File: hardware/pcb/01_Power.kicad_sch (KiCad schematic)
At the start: 11 parts, among them J1 USB_C_Receptacle_USB2.0_16P, U1 TLV62569DBV

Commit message: featt: make a 1.2 power rail from 3.3v
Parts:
- added C4, C7, C8: 22yF, symbol Device:C
- added C6: 10uF, symbol Device:C
- added L1: 2.2uH, symbol Device:L
- added R5, R6: 100k, symbol Device:R
- added U1: TLV62569DBV, Package_TO_SOT_SMD:SOT-23-5, symbol Regulator_Switching:TLV62569DBV
- renumbered U1 to U5
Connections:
- net +3V3: now also C6.1, U1.1 (EN), U1.4 (VIN)
- net GND: now also C4.2, C6.2, C7.2, R6.2, U1.2 (GND)
- new net: L1.1, U1.3 (SW)
- new net: C8.1, R5.2, R6.1, U1.5 (FB)
- new net +1V2: C4.1, C7.1, C8.2, L1.2, R5.1

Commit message: feat: the power circuit is fully made with all rails
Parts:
- added C10, C12: 1uF, symbol Device:C
- added C11, C13: 2.2uF, symbol Device:C
- added U2: TLV73325PDBV, Package_TO_SOT_SMD:SOT-23-5, symbol Regulator_Linear:TLV73325PDBV
- added U3: TLV73318PDBV, Package_TO_SOT_SMD:SOT-23-5, symbol Regulator_Linear:TLV73318PDBV
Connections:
- net +3V3: now also C10.1, C12.1, U2.1 (IN), U2.3 (EN), U3.1 (IN), U3.3 (EN)
- net GND: now also C10.2, C11.2, C12.2, C13.2, U2.2 (GND)
- new net +1V8: C13.1, U3.5 (OUT)
- new net +2V5: C11.1, U2.5 (OUT)

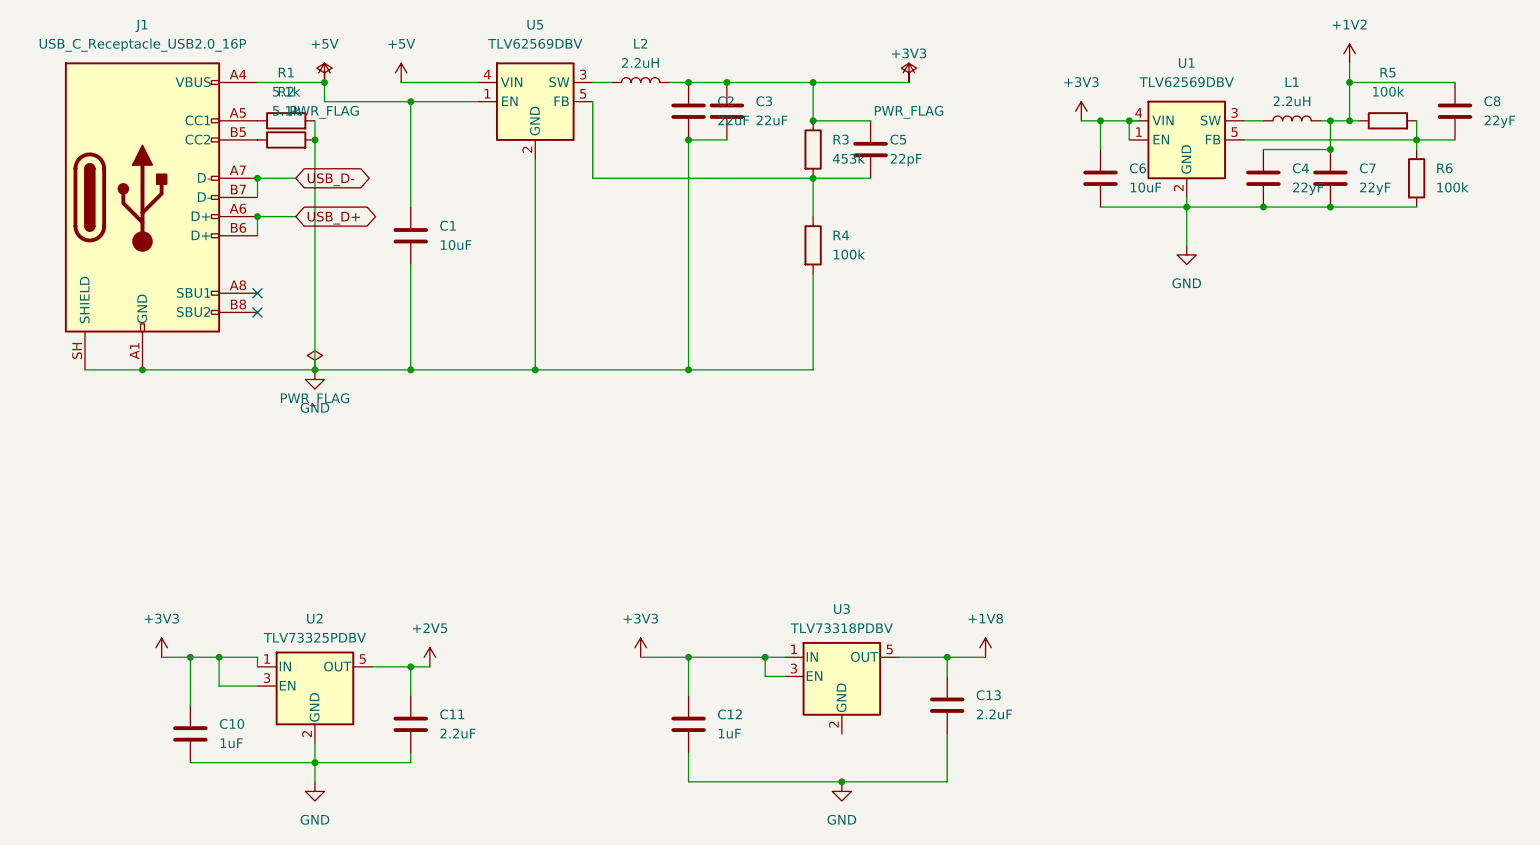
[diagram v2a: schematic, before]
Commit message: fix(power): resolve ERC violations and correct feedback capacitor values
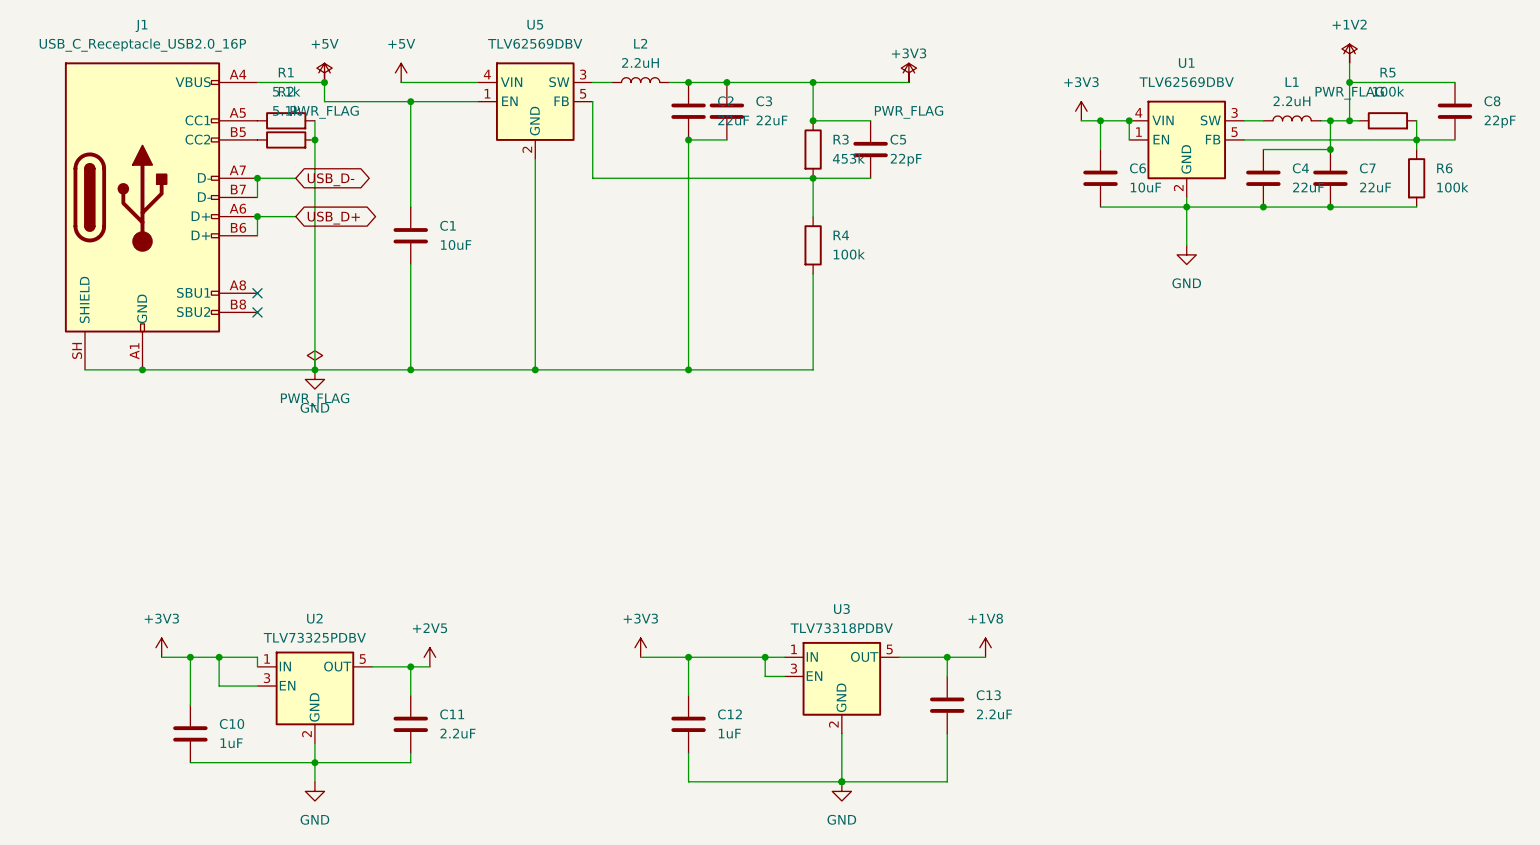
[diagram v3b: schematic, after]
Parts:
- C4, C7: value 22yF -> 22uF
- C8: value 22yF -> 22pF
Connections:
- net GND: now also U3.2 (GND)
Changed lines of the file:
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@@
 	(wire
 		(pts
-			(xy 153.67 72.39) (xy 154.94 72.39)
-		)
-		(stroke
-			(width 0)
-			(type default)
-		)
-	)
-	(wire
-		(pts
 			(xy 168.91 72.39) (xy 171.45 72.39)
 		)
@@
 			)
 		)
-		(property "Value" "22yF"
+		(property "Value" "22pF"
 			(at 200.66 72.3899 0)
 			(show_name no)
@@
 			)
 		)
-		(property "Value" "22yF"
+		(property "Value" "22uF"
 			(at 184.15 81.2799 0)
 			(show_name no)
@@
 			)
 		)
-		(property "Value" "22yF"
+		(property "Value" "22uF"
 			(at 175.26 81.2799 0)
 			(show_name no)
@@
 					(unit 1)
 				)
+			)
+		)
+	)
+	(wire
+		(pts
+			(xy 115.57 153.67) (xy 115.57 160.02)
+		)
+		(stroke
+			(width 0)
+			(type default)
+		)
+	)
+	(junction (at 115.57 160.02) (diameter 0) (color 0 0 0 0))
+	(symbol
+		(lib_id "power:PWR_FLAG")
+		(at 182.88 64.77 0)
+		(unit 1)
+		(exclude_from_sim no)
+		(in_bom yes)
+		(on_board yes)
+		(in_pos_files yes)
+		(dnp no)
+		(fields_autoplaced yes)
+		(property "Reference" "#FLG04"
+			(at 182.88 66.675 0)
+			(hide yes)
+			(show_name no)
+			(effects
+				(font
+					(size 1.27 1.27)
+				)
+			)
+		)
+		(property "Value" "PWR_FLAG"
+			(at 182.88 68.58 0)
+			(show_name no)
+			(effects
+				(font
+					(size 1.27 1.27)
+				)
+			)
+		)
+		(property "Footprint" ""
+			(at 182.88 64.77 0)
+			(hide yes)
+			(show_name no)
+			(effects
+				(font
+					(size 1.27 1.27)
+				)
+			)
+		)
+		(property "Datasheet" ""
+			(at 182.88 64.77 0)
+			(hide yes)
+			(show_name no)
+			(effects
+				(font
+					(size 1.27 1.27)
+				)
+			)
+		)
+		(property "Description" ""
+			(at 182.88 64.77 0)
+			(hide yes)
+			(show_name no)
+			(effects
+				(font
+					(size 1.27 1.27)
+				)
+			)
+		)
+		(pin "1"
+		)
+		(instances
+			(project "beanx5"
+				(path "/af63fa6e-973d-4760-8f53-35b43d2ef866/859f5aff-bcd5-4fba-93b3-4ce3a57d0421"
+					(reference "#FLG04")
+					(unit 1)
+				)

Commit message: feat: add power rails to the fpga gowin arora v family symbol
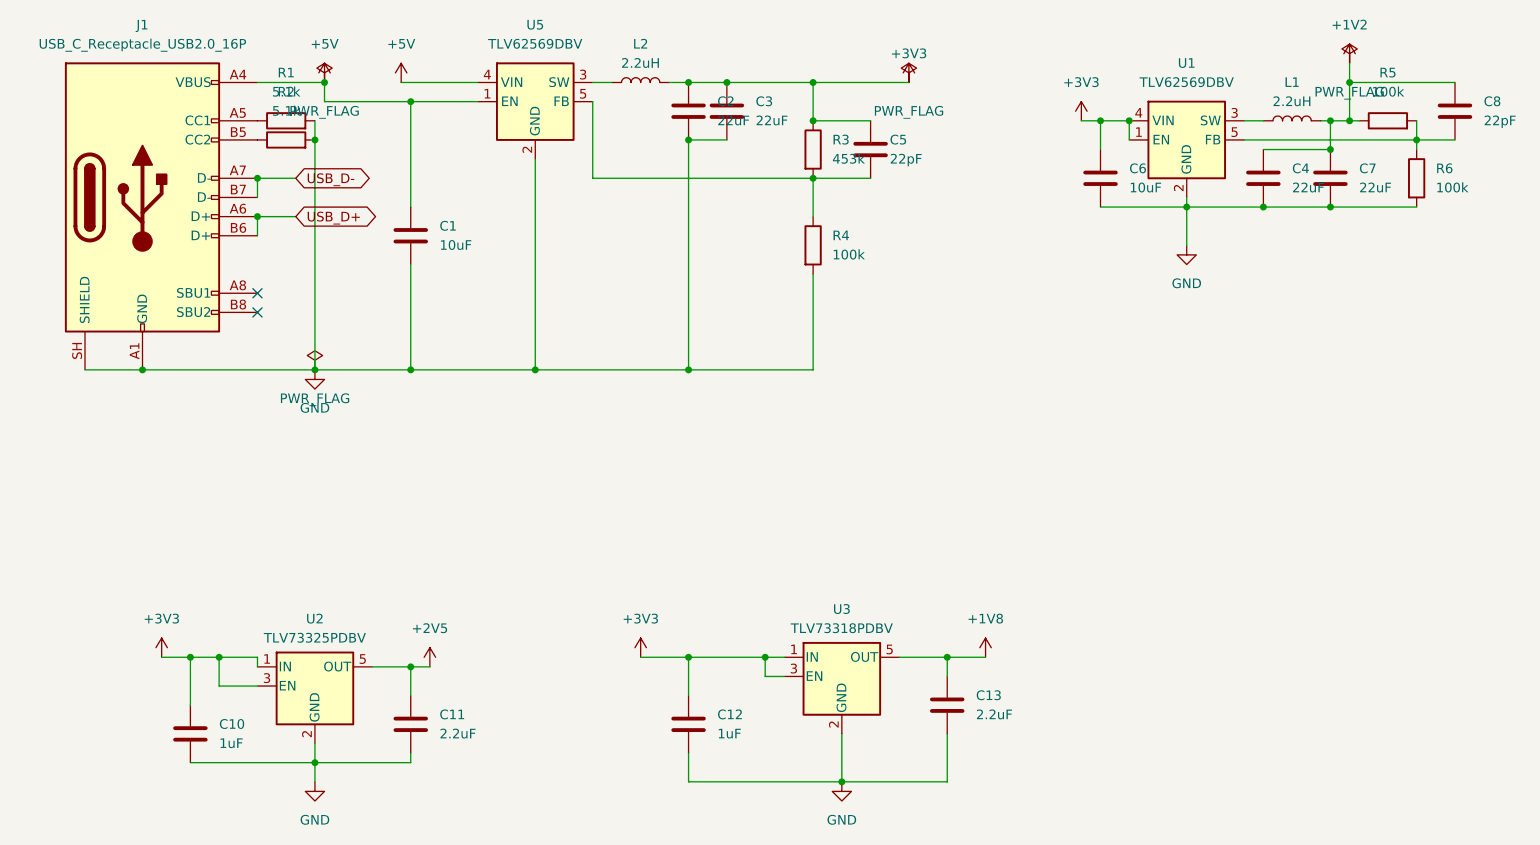
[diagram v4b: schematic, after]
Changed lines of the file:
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@@
 	(wire
 		(pts
-			(xy 45.72 105.41) (xy 74.93 105.41)
+			(xy 45.72 105.41) (xy 58.42 105.41)
 		)
 		(stroke
@@
 	(wire
 		(pts
+			(xy 58.42 69.85) (xy 67.31 69.85)
+		)
+		(stroke
+			(width 0)
+			(type default)
+		)
+	)
+	(wire
+		(pts
 			(xy 25.4 143.51) (xy 29.21 143.51)
 		)
@@
 	(wire
 		(pts
-			(xy 149.86 83.82) (xy 171.45 83.82)
+			(xy 149.86 83.82) (xy 161.29 83.82)
 		)
 		(stroke
@@
 	(wire
 		(pts
+			(xy 161.29 83.82) (xy 171.45 83.82)
+		)
+		(stroke
+			(width 0)
+			(type default)
+		)
+	)
+	(wire
+		(pts
 			(xy 95.25 67.31) (xy 100.33 67.31)
 		)
@@
 	(wire
 		(pts
-			(xy 46.99 69.85) (xy 67.31 69.85)
+			(xy 46.99 69.85) (xy 58.42 69.85)
 		)
 		(stroke
@@
 	(wire
 		(pts
+			(xy 58.42 105.41) (xy 74.93 105.41)
+		)
+		(stroke
+			(width 0)
+			(type default)
+		)
+	)
+	(wire
+		(pts
 			(xy 111.76 67.31) (xy 111.76 72.39)
 		)
@@
 	(wire
 		(pts
+			(xy 115.57 153.67) (xy 115.57 160.02)
+		)
+		(stroke
+			(width 0)
+			(type default)
+		)
+	)
+	(wire
+		(pts
 			(xy 74.93 77.47) (xy 74.93 105.41)
 		)
@@
 	)
 	(symbol
-		(lib_id "Device:C")
-		(at 171.45 80.01 0)
+		(lib_id "power:PWR_FLAG")
+		(at 182.88 64.77 0)
 		(unit 1)
 		(body_style 1)
@@
 		(dnp no)
 		(fields_autoplaced yes)
-		(property "Reference" "C4"
-			(at 175.26 78.7399 0)
+		(property "Reference" "#FLG04"
+			(at 182.88 66.675 0)
+			(hide yes)
 			(show_name no)
 			(do_not_autoplace no)
@@
 					(size 1.27 1.27)
 				)
-				(justify left)
 			)
 		)
-		(property "Value" "22uF"
-			(at 175.26 81.2799 0)
+		(property "Value" "PWR_FLAG"
+			(at 182.88 68.58 0)
 			(show_name no)
 			(do_not_autoplace no)
@@
 					(size 1.27 1.27)
 				)
-				(justify left)
 			)
 		)
 		(property "Footprint" ""
-			(at 172.4152 83.82 0)
+			(at 182.88 64.77 0)
 			(hide yes)
 			(show_name no)
@@
 		)
 		(property "Datasheet" ""
-			(at 171.45 80.01 0)
+			(at 182.88 64.77 0)
 			(hide yes)
 			(show_name no)
@@
 			)
 		)
-		(property "Description" "Unpolarized capacitor"
-			(at 171.45 80.01 0)
+		(property "Description" ""
+			(at 182.88 64.77 0)
 			(hide yes)
 			(show_name no)
@@
 			)
 		)
-		(pin "2"
-		)
 		(pin "1"
 		)
@@
 			(project "beanx5"
 				(path "/af63fa6e-973d-4760-8f53-35b43d2ef866/859f5aff-bcd5-4fba-93b3-4ce3a57d0421"
-					(reference "C4")
+					(reference "#FLG04")
 					(unit 1)
 				)
@@
 	)
 	(symbol
-		(lib_id "power:+1V8")
-		(at 134.62 143.51 0)
+		(lib_id "Device:C")
+		(at 171.45 80.01 0)
 		(unit 1)
 		(body_style 1)
@@
 		(dnp no)
 		(fields_autoplaced yes)
-		(property "Reference" "#PWR013"
-			(at 134.62 147.32 0)
-			(hide yes)
+		(property "Reference" "C4"
+			(at 175.26 78.7399 0)
 			(show_name no)
 			(do_not_autoplace no)
@@
 					(size 1.27 1.27)
 				)
+				(justify left)
 			)
 		)
-		(property "Value" "+1V8"
-			(at 134.62 138.43 0)
+		(property "Value" "22uF"
+			(at 175.26 81.2799 0)
 			(show_name no)
 			(do_not_autoplace no)
@@
 					(size 1.27 1.27)
 				)
+				(justify left)
 			)
 		)
 		(property "Footprint" ""
-			(at 134.62 143.51 0)
+			(at 172.4152 83.82 0)
 			(hide yes)
 			(show_name no)
@@
 		)
 		(property "Datasheet" ""
-			(at 134.62 143.51 0)
+			(at 171.45 80.01 0)
 			(hide yes)
 			(show_name no)
@@
 			)
 		)
-		(property "Description" "Power symbol creates a global label with name \"+1V8\""
-			(at 134.62 143.51 0)
+		(property "Description" "Unpolarized capacitor"
+			(at 171.45 80.01 0)
 			(hide yes)
 			(show_name no)
@@
 			)
 		)
+		(pin "2"
+		)
 		(pin "1"
 		)
@@
 			(project "beanx5"
 				(path "/af63fa6e-973d-4760-8f53-35b43d2ef866/859f5aff-bcd5-4fba-93b3-4ce3a57d0421"
-					(reference "#PWR013")
+					(reference "C4")
 					(unit 1)
 				)
@@
 	)
 	(symbol
-		(lib_id "Device:C")
-		(at 95.25 71.12 0)
+		(lib_id "power:+1V8")
+		(at 134.62 143.51 0)
 		(unit 1)
 		(body_style 1)
@@
 		(dnp no)
 		(fields_autoplaced yes)
-		(property "Reference" "C2"
-			(at 99.06 69.8499 0)
+		(property "Reference" "#PWR013"
+			(at 134.62 147.32 0)
+			(hide yes)
 			(show_name no)
 			(do_not_autoplace no)
@@
 					(size 1.27 1.27)
 				)
-				(justify left)
 			)
 		)
-		(property "Value" "22uF"
-			(at 99.06 72.3899 0)
+		(property "Value" "+1V8"
+			(at 134.62 138.43 0)
 			(show_name no)
 			(do_not_autoplace no)
@@
 					(size 1.27 1.27)
 				)
-				(justify left)
 			)
 		)
-		(property "Footprint" "Capacitor_SMD:C_0603_1608Metric"
-			(at 96.2152 74.93 0)
+		(property "Footprint" ""
+			(at 134.62 143.51 0)
 			(hide yes)
 			(show_name no)
@@
 		)
 		(property "Datasheet" ""
-			(at 95.25 71.12 0)
+			(at 134.62 143.51 0)
 			(hide yes)
 			(show_name no)
@@
 			)
 		)
-		(property "Description" "Unpolarized capacitor"
-			(at 95.25 71.12 0)
+		(property "Description" "Power symbol creates a global label with name \"+1V8\""
+			(at 134.62 143.51 0)
 			(hide yes)
 			(show_name no)
@@
 			)
 		)
-		(pin "2"
-		)
 		(pin "1"
 		)
@@
 			(project "beanx5"
 				(path "/af63fa6e-973d-4760-8f53-35b43d2ef866/859f5aff-bcd5-4fba-93b3-4ce3a57d0421"
-					(reference "C2")
+					(reference "#PWR013")
 					(unit 1)
 				)
@@
 		)
 	)
-	(wire
-		(pts
-			(xy 115.57 153.67) (xy 115.57 160.02)
-		)
-		(stroke
-			(width 0)
-			(type default)
-		)
-	)
-	(junction (at 115.57 160.02) (diameter 0) (color 0 0 0 0))
 	(symbol
-		(lib_id "power:PWR_FLAG")
-		(at 182.88 64.77 0)
+		(lib_id "Device:C")
+		(at 95.25 71.12 0)
 		(unit 1)
+		(body_style 1)
 		(exclude_from_sim no)
 		(in_bom yes)
@@
 		(dnp no)
 		(fields_autoplaced yes)
-		(property "Reference" "#FLG04"
-			(at 182.88 66.675 0)
-			(hide yes)
+		(property "Reference" "C2"
+			(at 99.06 69.8499 0)
 			(show_name no)
+			(do_not_autoplace no)
 			(effects
 				(font
 					(size 1.27 1.27)
 				)
+				(justify left)
 			)
 		)
-		(property "Value" "PWR_FLAG"
-			(at 182.88 68.58 0)
+		(property "Value" "22uF"
+			(at 99.06 72.3899 0)
 			(show_name no)
+			(do_not_autoplace no)
 			(effects
 				(font
 					(size 1.27 1.27)
 				)
+				(justify left)
 			)
 		)
-		(property "Footprint" ""
-			(at 182.88 64.77 0)
+		(property "Footprint" "Capacitor_SMD:C_0603_1608Metric"
+			(at 96.2152 74.93 0)
 			(hide yes)
 			(show_name no)
+			(do_not_autoplace no)
 			(effects
 				(font
@@
 		)
 		(property "Datasheet" ""
-			(at 182.88 64.77 0)
+			(at 95.25 71.12 0)
 			(hide yes)
 			(show_name no)
+			(do_not_autoplace no)
 			(effects
 				(font
@@
 			)
 		)
-		(property "Description" ""
-			(at 182.88 64.77 0)
+		(property "Description" "Unpolarized capacitor"
+			(at 95.25 71.12 0)
 			(hide yes)
 			(show_name no)
+			(do_not_autoplace no)
 			(effects
 				(font
@@
 			)
 		)
+		(pin "2"
+		)
 		(pin "1"
 		)
@@
 			(project "beanx5"
 				(path "/af63fa6e-973d-4760-8f53-35b43d2ef866/859f5aff-bcd5-4fba-93b3-4ce3a57d0421"
-					(reference "#FLG04")
+					(reference "C2")
 					(unit 1)
 				)
